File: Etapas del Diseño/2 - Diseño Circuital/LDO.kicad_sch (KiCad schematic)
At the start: 40 parts, among them J1 Vo, Q1 2N3904, Q2 2N3904, Q3 2N3904, Q4 2N3906, Q5 2N3906, Q6 2N3904, Q7 2N3904, Q8 IRF4905, U1 TL431LP, U2 LM358, U3 LM358, U4 LM358, U5 LM358, U6 LM358

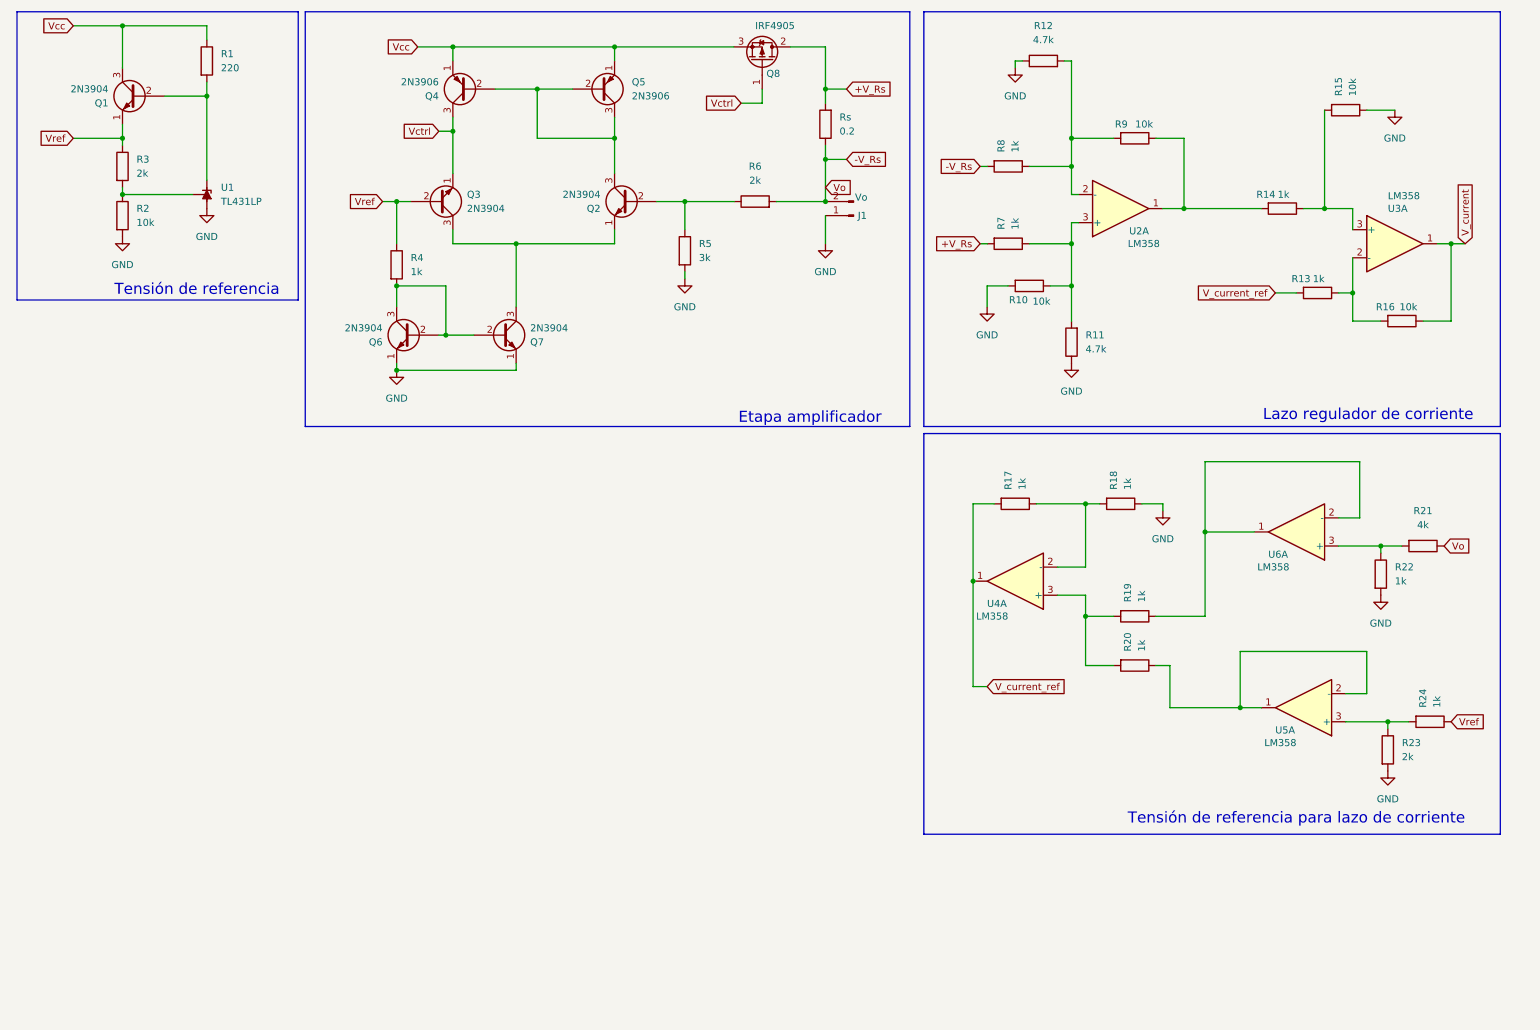
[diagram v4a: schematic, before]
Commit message: Esquematico con conmutador analógico, informe
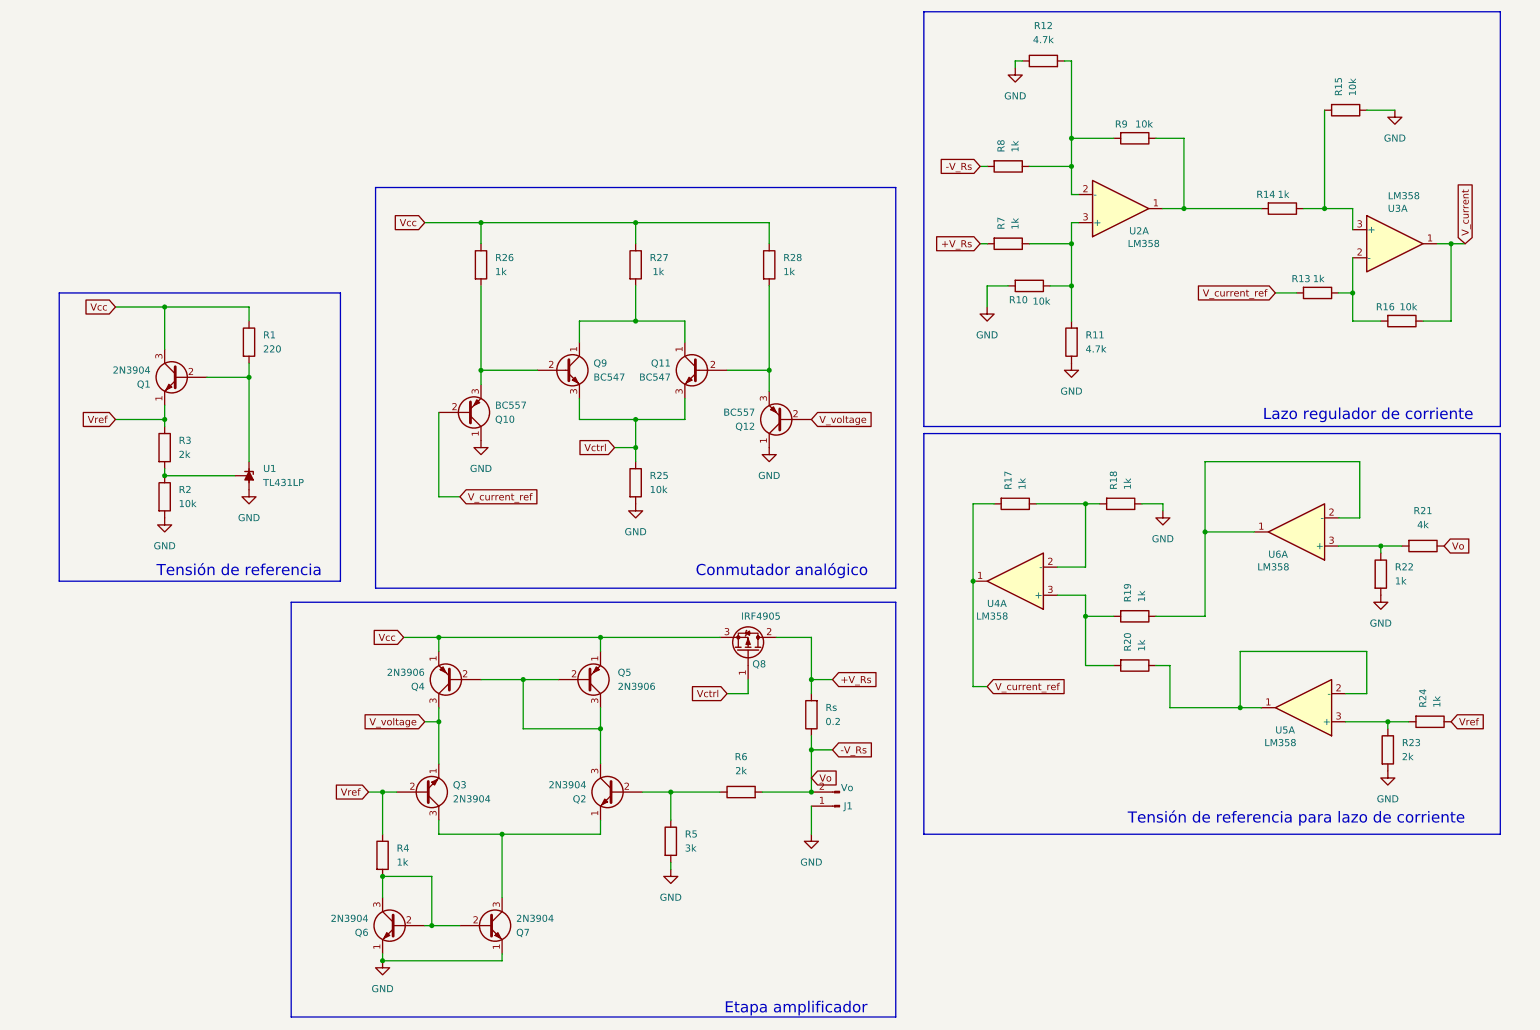
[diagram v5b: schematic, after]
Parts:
- added Q10, Q12: BC557, Package_TO_SOT_THT:TO-92_Inline, symbol Transistor_BJT:BC557
- added Q11, Q9: BC547, Package_TO_SOT_THT:TO-92_Inline, symbol Transistor_BJT:BC547
- added R25: 10k, symbol Device:R
- added R26, R27, R28: 1k, symbol Device:R
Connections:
- net GND: now also Q10.1 (C), Q12.1 (C), R25.2
- net V_current_ref: now also Q10.2 (B)
- net Vcc: now also R26.1, R27.1, R28.1
- net Vctrl: now also Q11.3 (E), Q9.3 (E), R25.1; no longer Q3.1 (E), Q4.3 (C)
- new net: Q11.2 (B), Q12.3 (E), R28.2
- new net: Q11.1 (C), Q9.1 (C), R27.2
- new net: Q10.3 (E), Q9.2 (B), R26.2
- new net V_voltage: Q12.2 (B), Q3.1 (E), Q4.3 (C)
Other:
- note added: "Conmutador analógico"
- moved on the sheet: J1, Q1, Q2, Q3, Q4, Q5, Q6, Q7, Q8, R1, R2, R3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

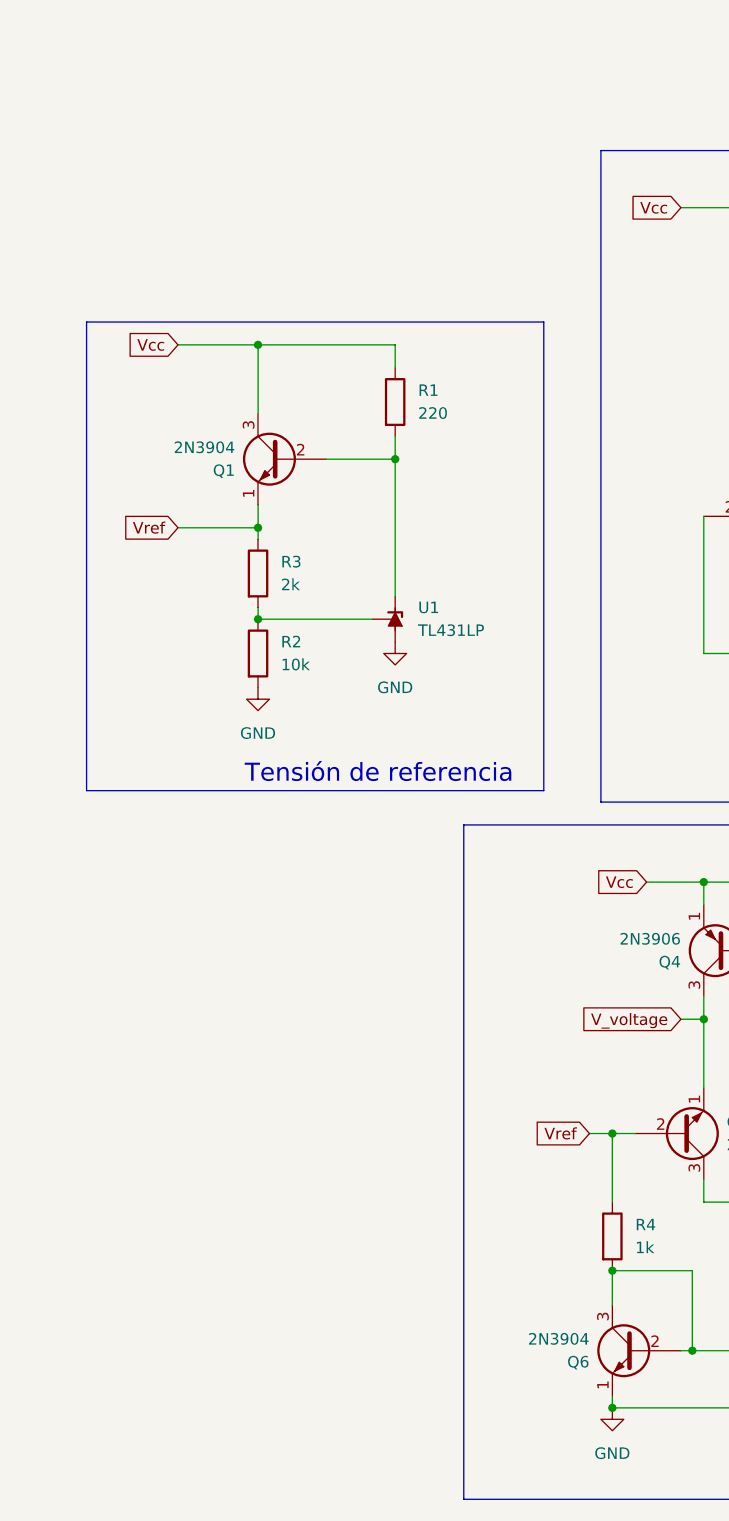
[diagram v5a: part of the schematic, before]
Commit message: Puntos de testeo, en esquematico
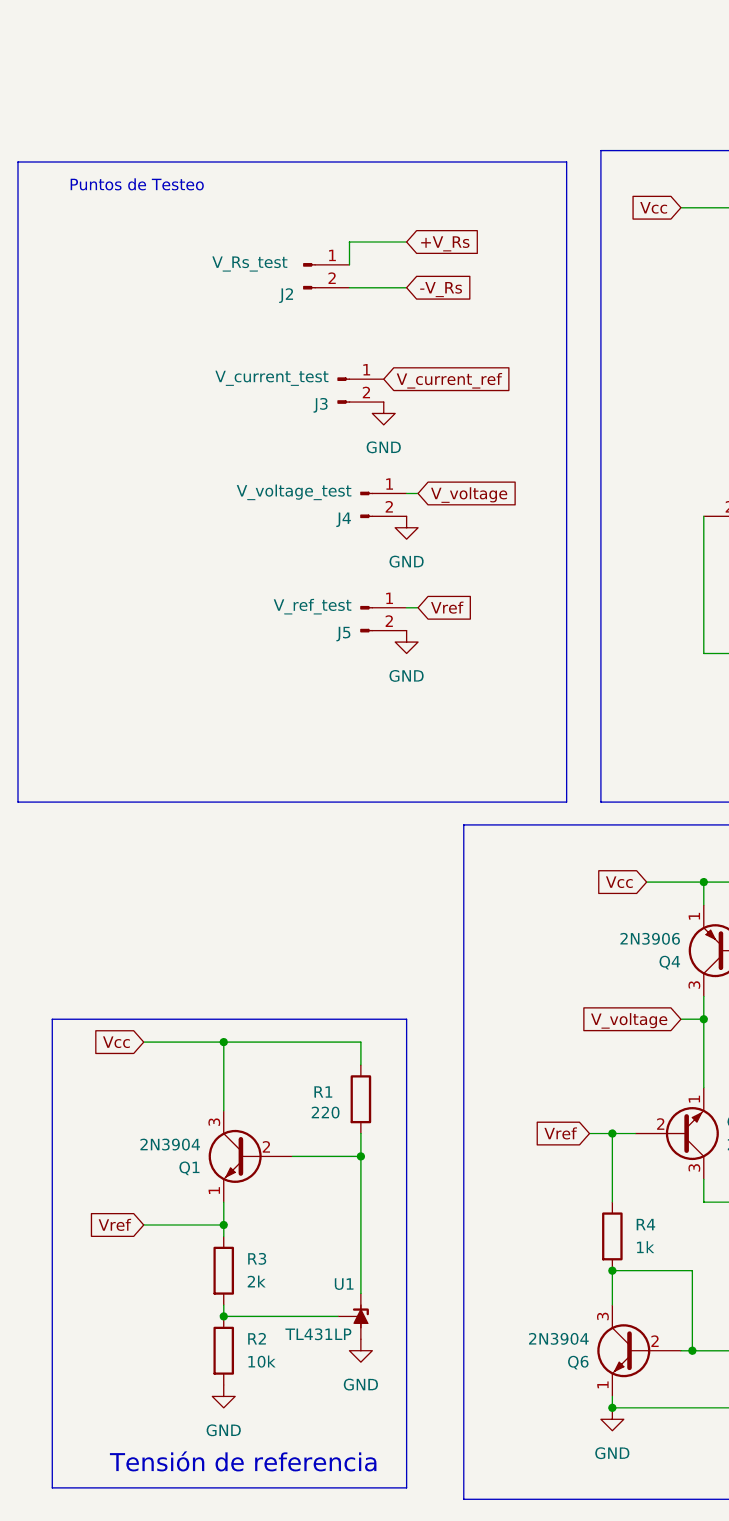
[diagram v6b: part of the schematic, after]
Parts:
- added J2: V_Rs_test, symbol Connector:Conn_01x02_Pin
- added J3: V_current_test, symbol Connector:Conn_01x02_Pin
- added J4: V_voltage_test, symbol Connector:Conn_01x02_Pin
- added J5: V_ref_test, symbol Connector:Conn_01x02_Pin
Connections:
- net +V_Rs: now also J2.1 (Pin_1)
- net -V_Rs: now also J2.2 (Pin_2)
- net GND: now also J3.2 (Pin_2), J4.2 (Pin_2), J5.2 (Pin_2)
- net V_current_ref: now also J3.1 (Pin_1)
- net V_voltage: now also J4.1 (Pin_1)
- net Vref: now also J5.1 (Pin_1)
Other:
- note added: "Puntos de Testeo"
- moved on the sheet: Q1, R1, R2, R3, U1

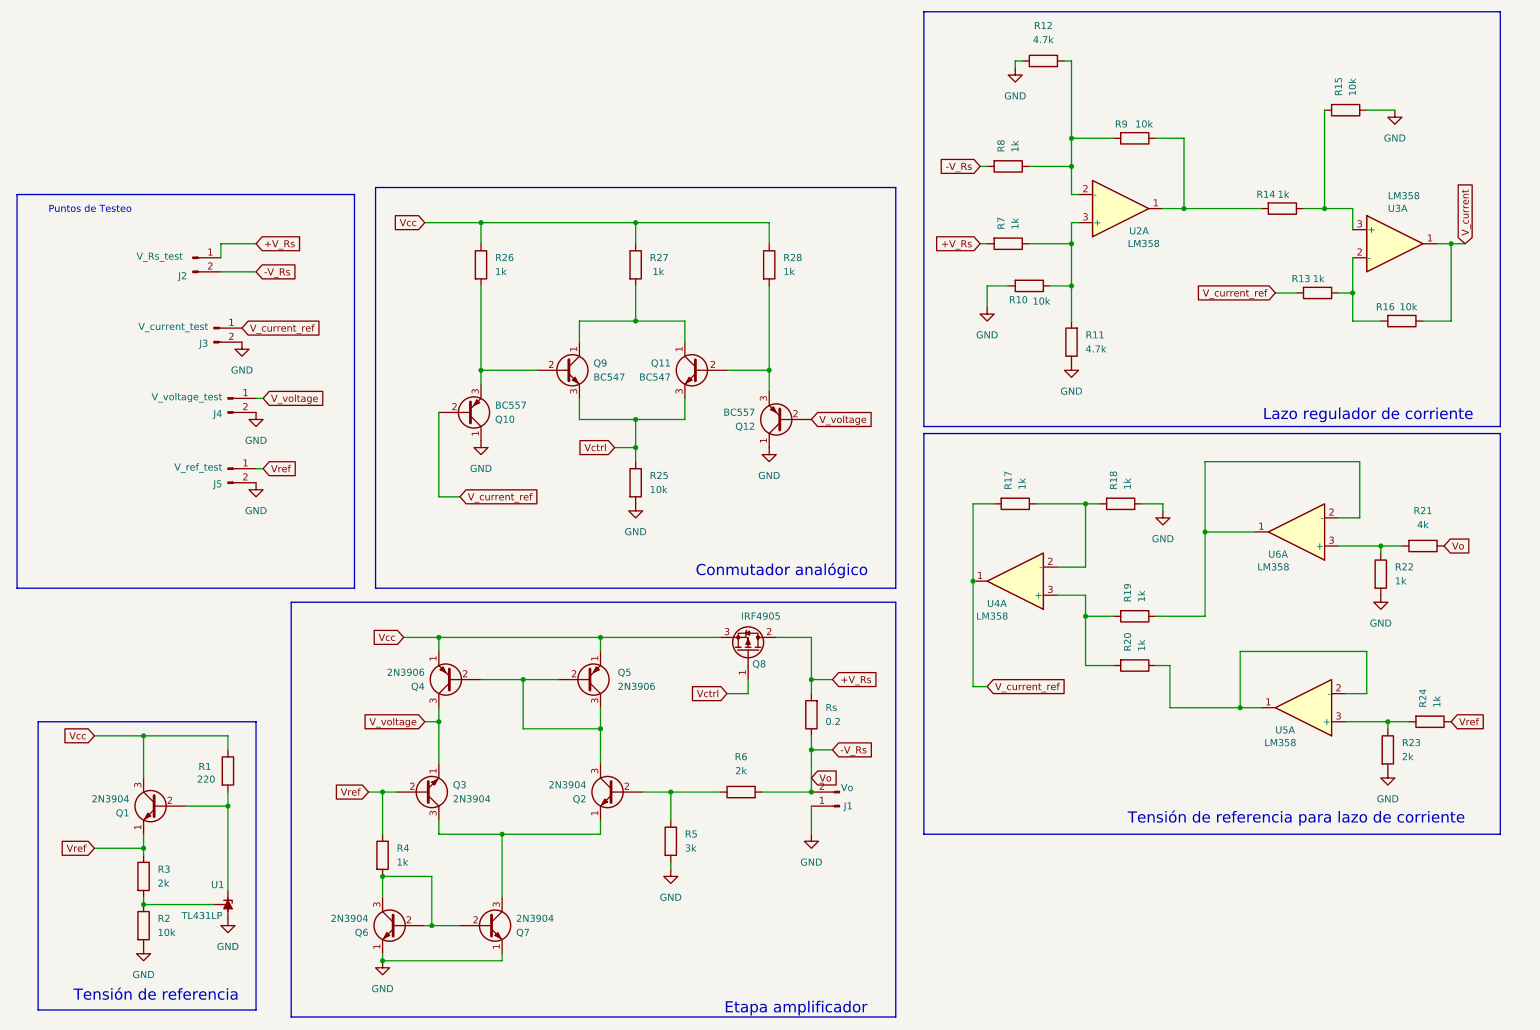
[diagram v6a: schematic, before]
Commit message: Agregue esquematicos en apendices
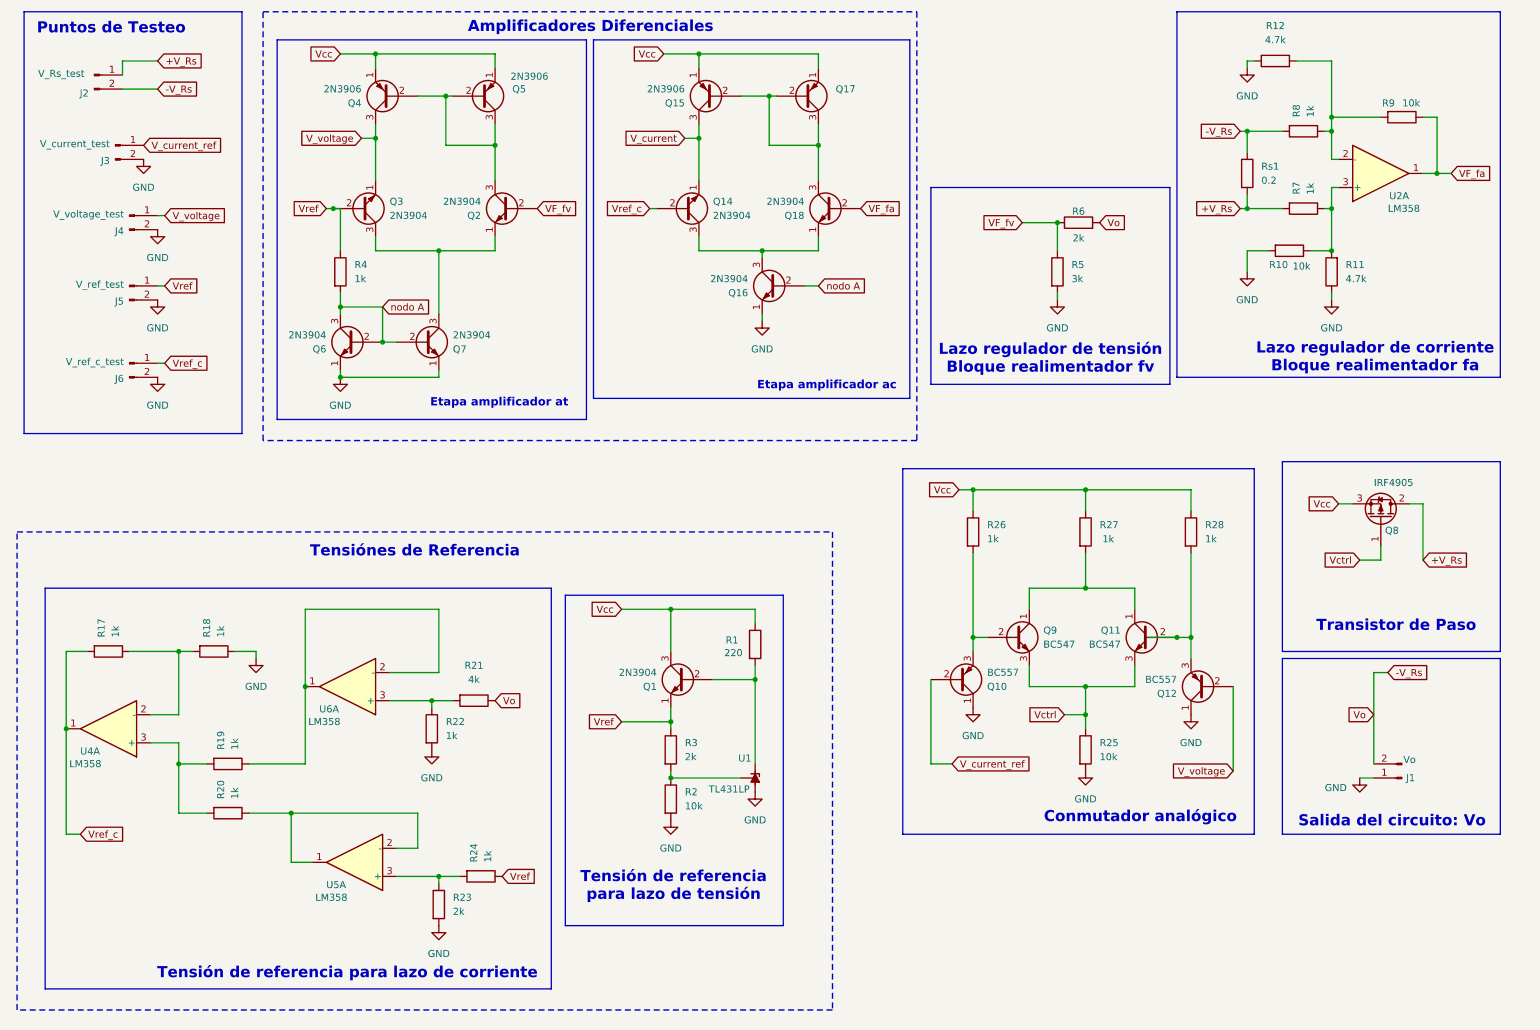
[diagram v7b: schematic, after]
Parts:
- removed R13, R14: 1k, symbol Device:R
- removed R15, R16: 10k, symbol Device:R
- removed Rs: 0.2, symbol Device:R
- removed U3: LM358, symbol Amplifier_Operational:LM358
- added J6: V_ref_c_test, symbol Connector:Conn_01x02_Pin
- added Q14, Q16, Q18: 2N3904, Package_TO_SOT_THT:TO-92_Inline, symbol Transistor_BJT:2N3904
- added Q15, Q17: 2N3906, Package_TO_SOT_THT:TO-92_Inline, symbol Transistor_BJT:2N3906
- added Rs1: 0.2, symbol Device:R
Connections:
- net +V_Rs: now also Rs1.2
- net -V_Rs: now also Rs1.1
- net GND: now also J6.2 (Pin_2), Q16.1 (E)
- net V_current: now also Q14.1 (E), Q15.3 (C)
- net V_current_ref: no longer R17.2, U4.1
- net Vcc: now also Q15.1 (E), Q17.1 (E)
- net VF_fa: now reaches R9.1, U2.1
- net VF_fa: now also Q18.2 (B)
- net nodo A: now reaches Q6.2 (B), Q6.3 (C), Q7.2 (B), R4.2
- net nodo A: now also Q16.2 (B)
- net VF_fv: now reaches Q2.2 (B), R5.1, R6.1
- new net: Q15.2 (B), Q17.2 (B), Q17.3 (C), Q18.3 (C)
- new net: Q14.3 (C), Q16.3 (C), Q18.1 (E)
- new net Vref_c: J6.1 (Pin_1), Q14.2 (B), R17.2, U4.1
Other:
- note added: "Amplificadores Diferenciales"
- note added: "Etapa amplificador ac"
- note added: "Etapa amplificador at"
- note added: "Lazo regulador de corriente Bloque realimentador fa"
- note added: "Lazo regulador de tensión Bloque realimentador fv"
- note added: "Salida del circuito: Vo"
- note added: "Tensión de referencia para lazo de tensión"
- note added: "Tensiónes de Referencia"
- note added: "Transistor de Paso"
- note removed: "Etapa amplificador"
- note removed: "Lazo regulador de corriente"
- note removed: "Tensión de referencia"
- moved on the sheet: J1, J2, J3, J4, J5, Q1, Q10, Q11, Q12, Q2, Q3, Q4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

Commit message: Actualizacion graficos y esquematico
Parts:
- removed R3: 2k, symbol Device:R
- added Q13: 2N3906, Package_TO_SOT_THT:TO-92_Inline, symbol Transistor_BJT:2N3906
- added Q19: 2N3904, Package_TO_SOT_THT:TO-92_Inline, symbol Transistor_BJT:2N3904
- R1: value 220 -> 2.2k
- R21: value 4k -> 1.4k
- R22: value 1k -> 1.1k
- R23: value 2k -> 800
- R24: value 1k -> 1.7k
- R26, R28: value 1k -> 10k
- R5: value 3k -> 2.2k
- R6: value 2k -> 2.2k
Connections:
- net +V_Rs: now also Q19.2 (B)
- net -V_Rs: now also Q19.1 (E)
- net Vcc: now also Q13.1 (E)
- net Vctrl: now also Q13.3 (C)
- net Vref: now also R2.1, U1.1 (REF)
- new net: Q13.2 (B), Q19.3 (C)
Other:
- note added: "Limitador de corriente"
- moved on the sheet: Q1, Q8, R1, R10, R11, R12, R17, R18, R19, R2, R20, R21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
